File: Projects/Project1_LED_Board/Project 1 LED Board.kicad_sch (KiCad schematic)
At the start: 0 parts

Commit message: setup sheet
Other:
- title: (none) -> Project 1 LED Board
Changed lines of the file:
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@@
 	(generator_version "9.0")
 	(paper "A4")
+	(title_block
+		(title "Project 1 LED Board")
+		(date "2026-01-10")
+		(rev "1")
+	)
 	(sheet_instances
 		(path "/"

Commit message: added symbols
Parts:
- added BT1: Battery_Cell, symbol Device:Battery_Cell
- added D1: LED, symbol Device:LED
- added R1: R, symbol Device:R
- added SW1: SW_DPDT_x2, symbol Switch:SW_DPDT_x2

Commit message: arranged symbols and associated footprints
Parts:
- BT1: footprint (none) -> Battery:BatteryHolder_Keystone_1058_1x2032
- D1: footprint (none) -> LED_THT:LED_D5.0mm
- R1: footprint (none) -> Resistor_THT:R_Axial_DIN0204_L3.6mm_D1.6mm_P7.62mm_Horizontal
- SW1: footprint (none) -> Button_Switch_THT:SW_SPST_Omron_B3F-40xx; symbol Switch:SW_DPDT_x2 -> Switch:SW_DPST_x2
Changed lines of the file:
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@@
 			)
 		)
-		(property "Footprint" ""
+		(property "Footprint" "Resistor_THT:R_Axial_DIN0204_L3.6mm_D1.6mm_P7.62mm_Horizontal"
 			(at 54.61 52.578 90)
 			(effects
@@
 	)
 	(symbol
-		(lib_id "Switch:SW_DPDT_x2")
+		(lib_id "Switch:SW_DPST_x2")
 		(at 68.58 50.8 0)
 		(unit 1)
@@
 		(fields_autoplaced yes)
 		(property "Reference" "SW1"
-			(at 68.58 41.91 0)
+			(at 68.58 44.45 0)
 			(effects
 				(font
@@
 		)
 		(property "Value" "SW_DPDT_x2"
-			(at 68.58 44.45 0)
-			(effects
-				(font
-					(size 1.27 1.27)
-				)
-			)
-		)
-		(property "Footprint" ""
+			(at 68.58 46.99 0)
+			(effects
+				(font
+					(size 1.27 1.27)
+				)
+			)
+		)
+		(property "Footprint" "Button_Switch_THT:SW_SPST_Omron_B3F-40xx"
 			(at 68.58 50.8 0)
 			(effects
@@
 			)
 		)
-		(property "Description" "Switch, dual pole double throw, separate symbols"
+		(property "Description" "Single Pole Single Throw (SPST) switch, separate symbol"
 			(at 68.58 50.8 0)
 			(effects
@@
 		(pin "4"
 		)
-		(pin "5"
-		)
 		(pin "3"
-		)
-		(pin "6"
 		)
 		(pin "2"
@@
 			)
 		)
-		(property "Footprint" ""
+		(property "Footprint" "Battery:BatteryHolder_Keystone_1058_1x2032"
 			(at 54.864 69.85 90)
 			(effects
@@
 			)
 		)
-		(property "Footprint" ""
+		(property "Footprint" "LED_THT:LED_D5.0mm"
 			(at 40.64 50.8 0)
 			(effects

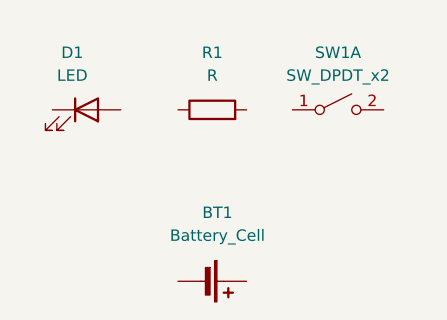
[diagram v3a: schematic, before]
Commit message: wired symbols together
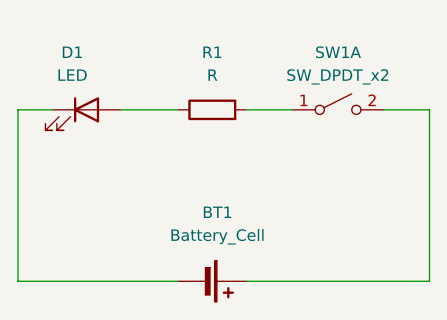
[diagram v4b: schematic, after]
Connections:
- net at R1.1: now also D1.2 (A)
- net at R1.2: now also SW1.1 (A)
- net at SW1.2 (B): now also BT1.1 (+)
- net at BT1.2 (-): now also D1.1 (K)
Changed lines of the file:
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@@
 		(rev "1")
+	)
+	(wire
+		(pts
+			(xy 78.74 50.8) (xy 73.66 50.8)
+		)
+		(stroke
+			(width 0)
+			(type default)
+		)
+	)
+	(wire
+		(pts
+			(xy 58.42 69.85) (xy 78.74 69.85)
+		)
+		(stroke
+			(width 0)
+			(type default)
+		)
+	)
+	(wire
+		(pts
+			(xy 78.74 69.85) (xy 78.74 50.8)
+		)
+		(stroke
+			(width 0)
+			(type default)
+		)
+	)
+	(wire
+		(pts
+			(xy 44.45 50.8) (xy 50.8 50.8)
+		)
+		(stroke
+			(width 0)
+			(type default)
+		)
+	)
+	(wire
+		(pts
+			(xy 58.42 50.8) (xy 63.5 50.8)
+		)
+		(stroke
+			(width 0)
+			(type default)
+		)
+	)
+	(wire
+		(pts
+			(xy 33.02 69.85) (xy 50.8 69.85)
+		)
+		(stroke
+			(width 0)
+			(type default)
+		)
+	)
+	(wire
+		(pts
+			(xy 36.83 50.8) (xy 33.02 50.8)
+		)
+		(stroke
+			(width 0)
+			(type default)
+		)
+	)
+	(wire
+		(pts
+			(xy 33.02 50.8) (xy 33.02 69.85)
+		)
+		(stroke
+			(width 0)
+			(type default)
+		)
 	)
 	(symbol
